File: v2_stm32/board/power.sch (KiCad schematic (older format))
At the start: 22 parts

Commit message: Switched to 64 pin STM32F103. Assigned pins
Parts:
- U?: symbol MP2451DT-LF-P:MP2451DT-LF-P -> lathecontrol_stm32-rescue:MP2451DT-LF-P-MP2451DT-LF-P
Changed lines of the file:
@@
 5V to 3.3V LDO
 $Comp
-L MP2451DT-LF-P:MP2451DT-LF-P U?
+L lathecontrol_stm32-rescue:MP2451DT-LF-P-MP2451DT-LF-P U?
 U 1 1 602ADA2D
 P 1600 2050

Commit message: Pins
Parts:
- gave numbers to parts that had none: 22
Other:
- note added: "DCDC-Converter 9...15V -> 5V"
- moved on the sheet: C14, C15, C16, C17, C18, C19, C20, C21, D1, D2, L1, R10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

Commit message: Added connectors
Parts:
- removed C15, C20: C, symbol Device:C
- removed C21: 33p, Capacitor_SMD:C_0603_1608Metric, symbol Device:C
- removed U4: MP2451DT-LF-P, MP2451DT-LF-P:MP2451DT-LF-P, symbol lathecontrol_stm32-rescue:MP2451DT-LF-P-MP2451DT-LF-P
- added C14, C19: 10u, Capacitor_SMD:C_0805_2012Metric, symbol Device:C
- added C16: 30p, Capacitor_SMD:C_0603_1608Metric, symbol Device:C
- added U2: MP2451DT-LF-Z, Package_TO_SOT_SMD:SOT-23-6, symbol Lathecontrol_STM32:MP2451DT-LF-Z
- C17: value 2u2 -> 22u; footprint Capacitor_SMD:C_0603_1608Metric -> Capacitor_SMD:C_0805_2012Metric; LCSC C23630 -> C45783
- L1: value L -> 4U7; footprint (none) -> Lathecontrol_STM32:L_3012_SMD3.0x3.0x1.2mm; LCSC (none) -> C83415; MFR_Part (none) -> SWPA3012S4R7MT
- renumbered C14 to C15, C16 to C18, C18 to C20, C19 to C21, D2 to D1, D1 to D2, R14 to R13, R15 to R14, R16 to R15, R17 to R16, R10 to R17, R13 to R18, U2 to U3, U3 to U4
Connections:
- wire segments 54 -> 53
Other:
- moved on the sheet: C15, D1, L1, R11, R12, R13, R14, R15, R16

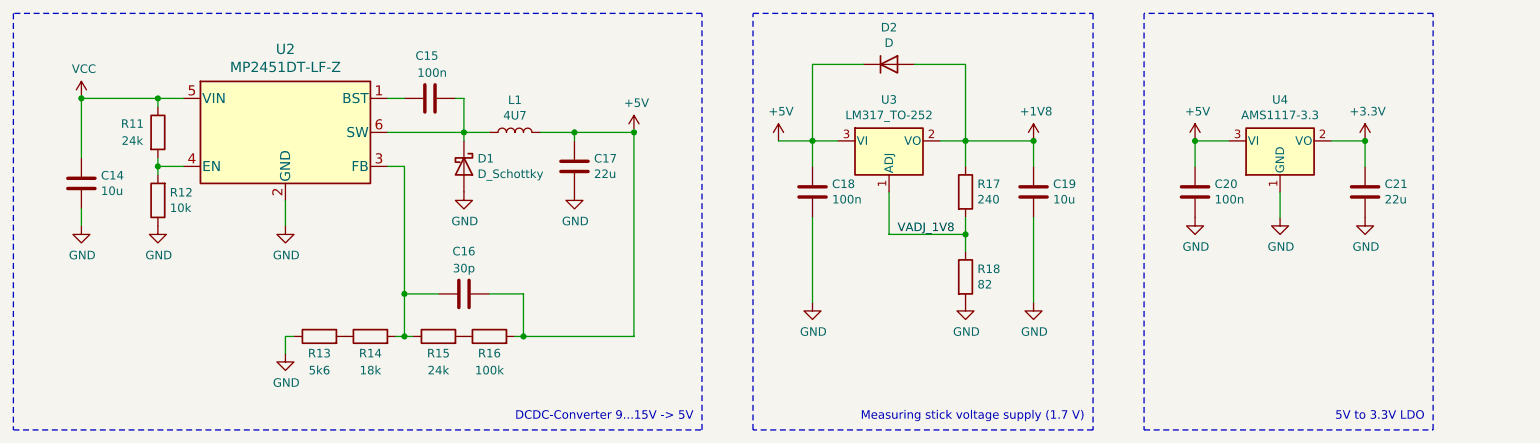
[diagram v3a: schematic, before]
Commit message: Added LEDs
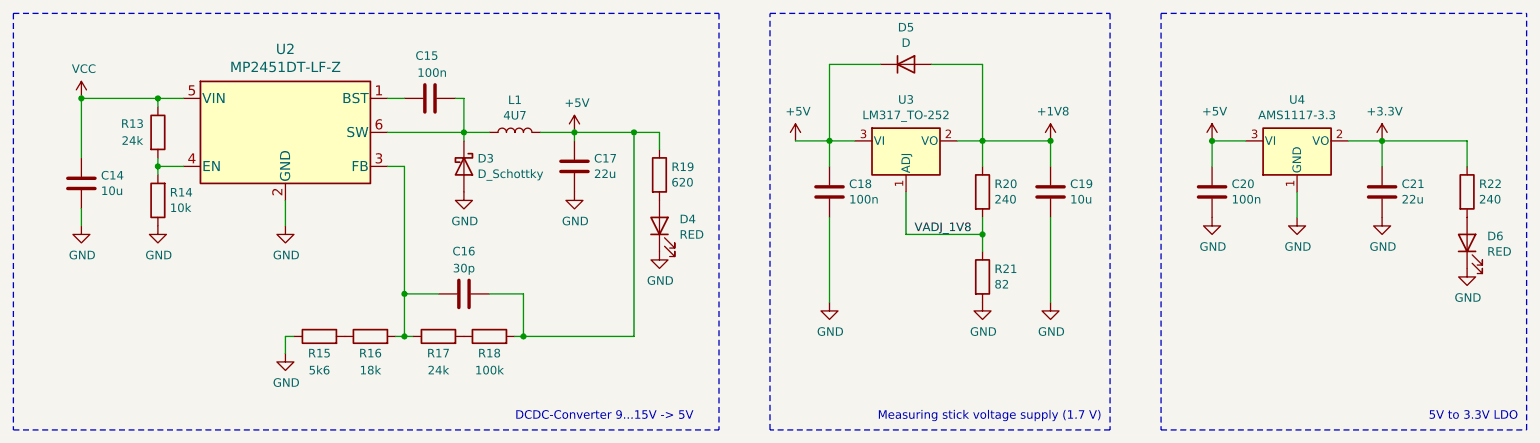
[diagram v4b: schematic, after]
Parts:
- added D4, D6: RED, LED_SMD:LED_0603_1608Metric, symbol Device:LED
- added R19: 620, Resistor_SMD:R_0603_1608Metric, symbol Device:R
- added R22: 240, Resistor_SMD:R_0603_1608Metric, symbol Device:R
- renumbered D1 to D3, D2 to D5, R11 to R13, R12 to R14, R13 to R15, R14 to R16, R15 to R17, R16 to R18, R17 to R20, R18 to R21
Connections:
- net +3V3: now also R22.1
- net +5V: now also R19.1
- net GND: now also D4.1 (K), D6.1 (K)
- new net: D6.2 (A), R22.2
- new net: D4.2 (A), R19.2
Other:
- moved on the sheet: C18, C19, C20, C21, D5, R20, R21, U3, U4

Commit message: Schematic finished (V0.1), Added footprints
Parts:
- D3: footprint (none) -> Diode_SMD:D_SMA; LCSC (none) -> C14996
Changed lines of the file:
@@
 F 0 "D3" V 3654 1930 50  0000 L CNN
 F 1 "D_Schottky" V 3745 1930 50  0000 L CNN
-F 2 "" H 3700 1850 50  0001 C CNN
-F 3 "~" H 3700 1850 50  0001 C CNN
+F 2 "Diode_SMD:D_SMA" H 3700 1850 50  0001 C CNN
+F 3 "https://datasheet.lcsc.com/szlcsc/1903041730_MDD-Jiangsu-Yutai-Elec-SS210_C14996.pdf" H 3700 1850 50  0001 C CNN
+F 4 "C14996" V 3700 1850 50  0001 C CNN "LCSC"
 	1    3700 1850
 	0    1    1    0

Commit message: More routing
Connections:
- net 5VRAW: now reaches C15.2, D3.1 (K), L1.1, U2.6 (SW)
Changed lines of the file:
@@
 Wire Wire Line
 	4850 1650 4850 1750
+Text Label 3300 1650 0    50   ~ 0
+5VRAW
 $EndSCHEMATC

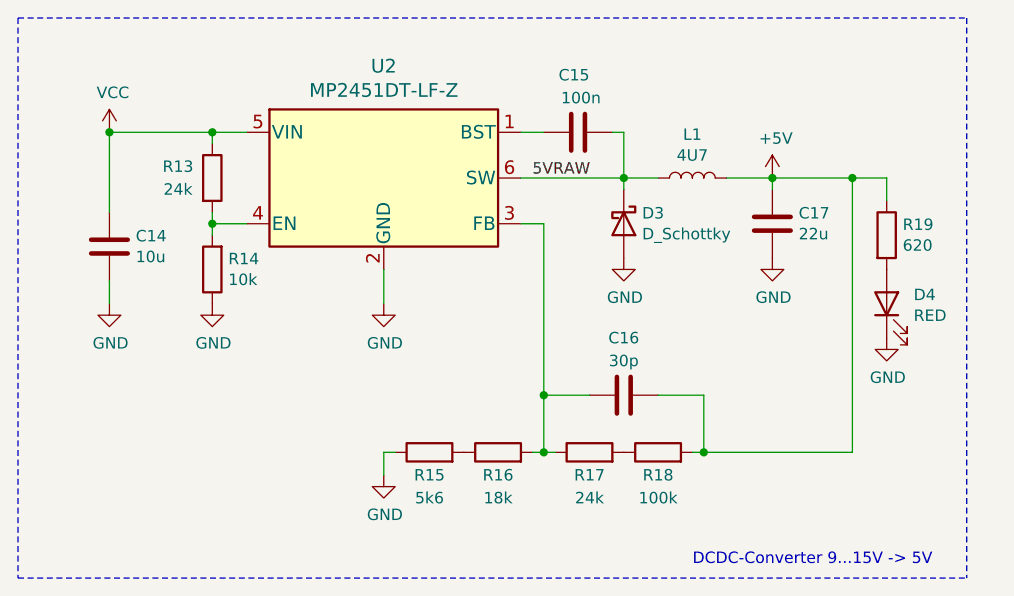
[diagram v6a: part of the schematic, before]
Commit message: MP2451 Routing according to datasheet
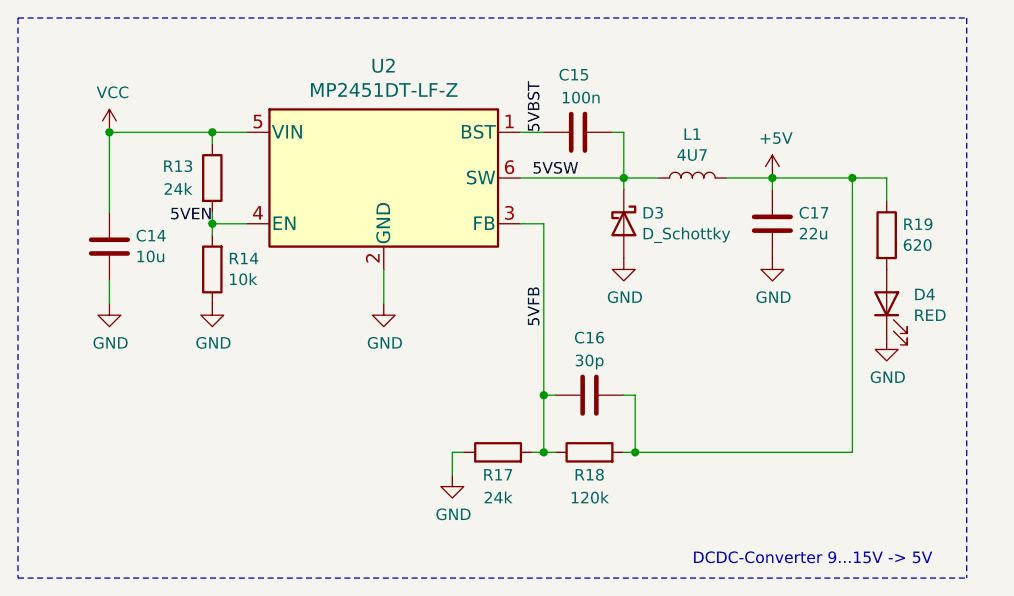
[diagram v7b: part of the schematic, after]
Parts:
- removed R15: 5k6, Resistor_SMD:R_0603_1608Metric, symbol Device:R
- removed R16: 18k, Resistor_SMD:R_0603_1608Metric, symbol Device:R
- D3: footprint Diode_SMD:D_SMA -> Diode_SMD:D_SOD-123; LCSC C14996 -> C8598
- R18: value 100k -> 120k; LCSC C25803 -> C25808
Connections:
- net GND: now also R17.1
- net 5VBST: now reaches C15.1, U2.1 (BST)
- net 5VEN: now reaches R13.2, R14.2, U2.4 (EN)
- net 5VFB: now reaches C16.1, U2.3 (FB)
- net 5VFB: now also R17.2, R18.1; no longer R17.1
- net 5VRAW renamed 5VSW
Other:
- moved on the sheet: C16, R17, R18
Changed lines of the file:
@@
 L Device:C C?
 U 1 1 6046279B
-P 3700 2600
+P 3550 2600
 AR Path="/6025D9E2/6046279B" Ref="C?"  Part="1"
 AR Path="/6025D9E2/6025E7C0/6046279B" Ref="C?"  Part="1"
@@
 AR Path="/6046279B" Ref="C?"  Part="1"
 AR Path="/60278C87/6046279B" Ref="C16"  Part="1"
-F 0 "C16" V 3950 2600 50  0000 C CNN
-F 1 "30p" V 3850 2600 50  0000 C CNN
-F 2 "Capacitor_SMD:C_0603_1608Metric" H 3738 2450 50  0001 C CNN
-F 3 "https://datasheet.lcsc.com/szlcsc/1809300925_Samsung-Electro-Mechanics-CL10C300JB8NNNC_C22397.pdf" H 3700 2600 50  0001 C CNN
-F 4 "C22397" H 3700 2600 50  0001 C CNN "LCSC"
-	1    3700 2600
+F 0 "C16" V 3800 2600 50  0000 C CNN
+F 1 "30p" V 3700 2600 50  0000 C CNN
+F 2 "Capacitor_SMD:C_0603_1608Metric" H 3588 2450 50  0001 C CNN
+F 3 "https://datasheet.lcsc.com/szlcsc/1809300925_Samsung-Electro-Mechanics-CL10C300JB8NNNC_C22397.pdf" H 3550 2600 50  0001 C CNN
+F 4 "C22397" H 3550 2600 50  0001 C CNN "LCSC"
+	1    3550 2600
 	0    -1   -1   0
 $EndComp
@@
 $EndComp
 Connection ~ 4700 1650
-Wire Wire Line
-	4050 2850 4000 2850
-Connection ~ 4050 2850
-Wire Wire Line
-	4050 2600 4050 2850
-Wire Wire Line
-	3850 2600 4050 2600
+Connection ~ 3750 2850
+Wire Wire Line
+	3750 2600 3750 2850
 Wire Wire Line
 	3350 2600 3350 2850
 Connection ~ 3350 2600
-Wire Wire Line
-	3550 2600 3350 2600
 Connection ~ 3350 2850
 Wire Wire Line
@@
 Connection ~ 4350 1650
 Wire Wire Line
-	4700 2850 4050 2850
+	4700 2850 3750 2850
 Wire Wire Line
 	4700 1650 4700 2850
@@
 	4350 1650 4700 1650
 Wire Wire Line
-	2650 2850 2650 2950
-Wire Wire Line
-	2700 2850 2650 2850
-$Comp
-L Device:R R18
-U 1 1 60355196
-P 3850 2850
-F 0 "R18" V 3750 2850 50  0000 C CNN
-F 1 "100k" V 3650 2850 50  0000 C CNN
-F 2 "Resistor_SMD:R_0603_1608Metric" V 3780 2850 50  0001 C CNN
-F 3 "~" H 3850 2850 50  0001 C CNN
-F 4 "C25803" V 3850 2850 50  0001 C CNN "LCSC"
-	1    3850 2850
-	0    -1   -1   0
-$EndComp
+	2950 2850 2950 2950
+Wire Wire Line
+	3000 2850 2950 2850
 $Comp
 L Device:R R17
 U 1 1 60354B49
-P 3550 2850
-F 0 "R17" V 3450 2850 50  0000 C CNN
-F 1 "24k" V 3350 2850 50  0000 C CNN
-F 2 "Resistor_SMD:R_0603_1608Metric" V 3480 2850 50  0001 C CNN
-F 3 "~" H 3550 2850 50  0001 C CNN
-F 4 "C23352" V 3550 2850 50  0001 C CNN "LCSC"
-	1    3550 2850
+P 3150 2850
+F 0 "R17" V 3050 2850 50  0000 C CNN
+F 1 "24k" V 2950 2850 50  0000 C CNN
+F 2 "Resistor_SMD:R_0603_1608Metric" V 3080 2850 50  0001 C CNN
+F 3 "~" H 3150 2850 50  0001 C CNN
+F 4 "C23352" V 3150 2850 50  0001 C CNN "LCSC"
+	1    3150 2850
 	0    -1   -1   0
 $EndComp
@@
 	1050 950  1050 3400
 $Comp
-L Device:R R16
-U 1 1 6035D5BD
-P 3150 2850
-F 0 "R16" V 3050 2850 50  0000 C CNN
-F 1 "18k" V 2950 2850 50  0000 C CNN
-F 2 "Resistor_SMD:R_0603_1608Metric" V 3080 2850 50  0001 C CNN
-F 3 "~" H 3150 2850 50  0001 C CNN
-F 4 "C25810" V 3150 2850 50  0001 C CNN "LCSC"
-	1    3150 2850
-	0    -1   -1   0
-$EndComp
-$Comp
 L Device:R R13
 U 1 1 603530B1
@@
 $EndComp
 $Comp
-L Device:R R15
-U 1 1 6034E6A4
-P 2850 2850
-F 0 "R15" V 2750 2850 50  0000 C CNN
-F 1 "5k6" V 2650 2850 50  0000 C CNN
-F 2 "Resistor_SMD:R_0603_1608Metric" V 2780 2850 50  0001 C CNN
-F 3 "~" H 2850 2850 50  0001 C CNN
-F 4 "C23189" V 2850 2850 50  0001 C CNN "LCSC"
-	1    2850 2850
-	0    -1   -1   0
-$EndComp
-$Comp
 L power:+5V #PWR075
 U 1 1 6033586F
@@
 L power:GND #PWR073
 U 1 1 60325786
-P 2650 2950
-F 0 "#PWR073" H 2650 2700 50  0001 C CNN
-F 1 "GND" H 2655 2777 50  0000 C CNN
-F 2 "" H 2650 2950 50  0001 C CNN
-F 3 "" H 2650 2950 50  0001 C CNN
-	1    2650 2950
+P 2950 2950
+F 0 "#PWR073" H 2950 2700 50  0001 C CNN
+F 1 "GND" H 2955 2777 50  0000 C CNN
+F 2 "" H 2950 2950 50  0001 C CNN
+F 3 "" H 2950 2950 50  0001 C CNN
+	1    2950 2950
 	1    0    0    -1
 $EndComp
@@
 F 0 "D3" V 3654 1930 50  0000 L CNN
 F 1 "D_Schottky" V 3745 1930 50  0000 L CNN
-F 2 "Diode_SMD:D_SMA" H 3700 1850 50  0001 C CNN
-F 3 "https://datasheet.lcsc.com/szlcsc/1903041730_MDD-Jiangsu-Yutai-Elec-SS210_C14996.pdf" H 3700 1850 50  0001 C CNN
-F 4 "C14996" V 3700 1850 50  0001 C CNN "LCSC"
+F 2 "Diode_SMD:D_SOD-123" H 3700 1850 50  0001 C CNN
+F 3 "https://datasheet.lcsc.com/szlcsc/Changjiang-Electronics-Tech-CJ-B5819W_C8598.pdf" H 3700 1850 50  0001 C CNN
+F 4 "C8598" V 3700 1850 50  0001 C CNN "LCSC"
 	1    3700 1850
 	0    1    1    0
@@
 	4850 1650 4850 1750
 Text Label 3300 1650 0    50   ~ 0
-5VRAW
+5VSW
+Text Label 3350 2300 1    50   ~ 0
+5VFB
+Text Label 1900 1850 2    50   ~ 0
+5VEN
+$Comp
+L Device:R R18
+U 1 1 60355196
+P 3550 2850
+F 0 "R18" V 3450 2850 50  0000 C CNN
+F 1 "120k" V 3350 2850 50  0000 C CNN
+F 2 "Resistor_SMD:R_0603_1608Metric" V 3480 2850 50  0001 C CNN
+F 3 "~" H 3550 2850 50  0001 C CNN
+F 4 "C25808" V 3550 2850 50  0001 C CNN "LCSC"
+	1    3550 2850
+	0    -1   -1   0
+$EndComp
+Wire Wire Line
+	3700 2850 3750 2850
+Wire Wire Line
+	3400 2600 3350 2600
+Wire Wire Line
+	3700 2600 3750 2600
+Text Label 3350 1450 1    50   ~ 0
+5VBST
 $EndSCHEMATC

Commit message: More PCB design
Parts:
- removed C17: 22u, Capacitor_SMD:C_0805_2012Metric, symbol Device:C
- added C10, C11: 10u, Capacitor_SMD:C_0805_2012Metric, symbol Device:C
- added C8: 1u, Inductor_SMD:L_0402_1005Metric, symbol Device:C
- added C9: 10n, Inductor_SMD:L_0402_1005Metric, symbol Device:C
- added D7: D_Schottky, Diode_SMD:D_SOD-123, symbol Device:D_Schottky
- added FB1: 600 @ 600MHz, Inductor_SMD:L_0805_2012Metric, symbol Device:Ferrite_Bead
- added L2: 39n, Inductor_SMD:L_0402_1005Metric, symbol Device:L
- added Q2, Q3: AO3401A, Package_TO_SOT_SMD:SOT-23, symbol Transistor_FET:AO3401A
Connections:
- net +3V3: now also L2.1
- net +5V: now also C10.1, C11.1, D7.2 (A), Q3.2 (S)
- net GND: now also C10.2, C11.2, C8.2, C9.2, Q2.1 (G), Q3.1 (G)
- net VCC: now also FB1.1
- new net +3.3VA: C8.1, C9.1, L2.2
- new net IN_+5V: Q3.3 (D)
- new net IN_VCC: Q2.3 (D)
- new net VCC_MID: D7.1 (K), FB1.2, Q2.2 (S)
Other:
- note added: "Analog Filtering"
- moved on the sheet: C14, C15, C16, C18, C19, C20, C21, D3, D4, D5, D6, L1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
